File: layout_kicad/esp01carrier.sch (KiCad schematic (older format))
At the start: 17 parts, among them J1 ESP-01, J2 REED1, J3 REED2, J4 Vin 5V, U1 CD74HCT86E, U2 SN74HCT32N, U3 HT7333

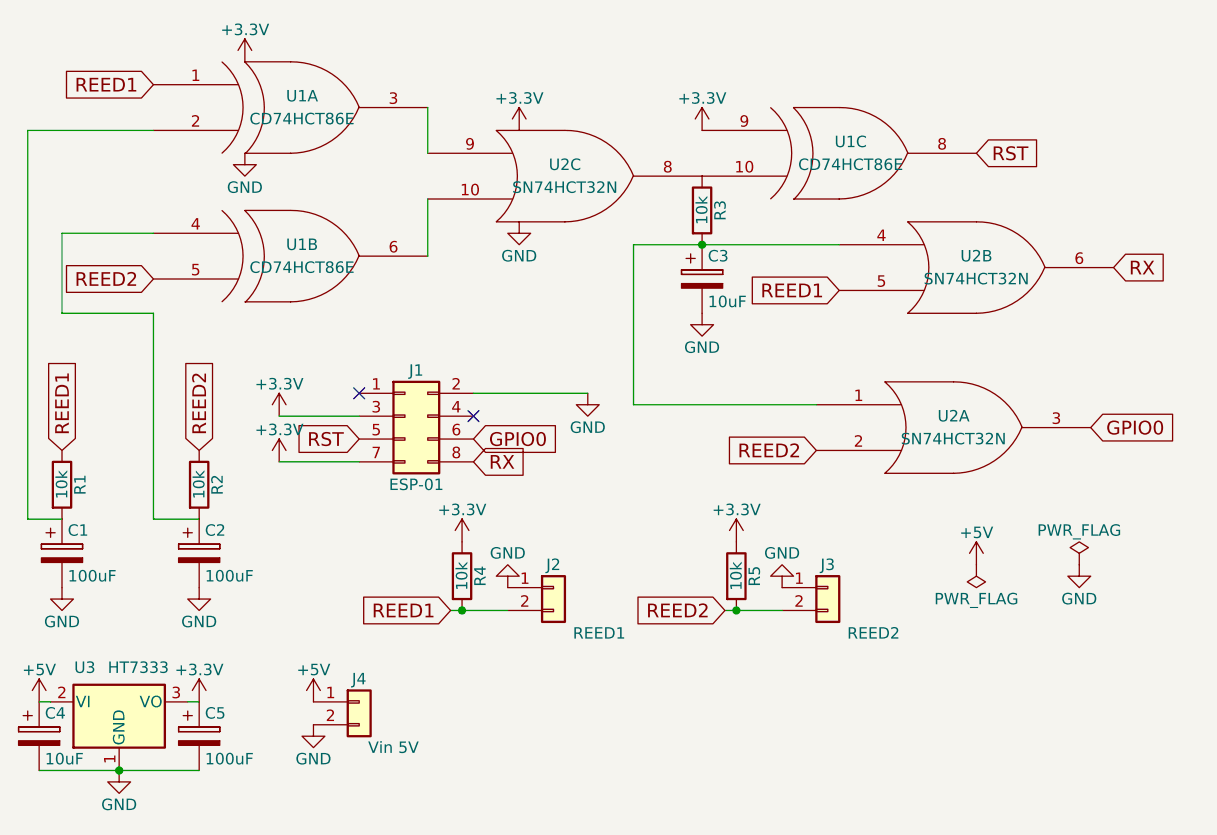
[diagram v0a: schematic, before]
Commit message: Change RC-curcuits to reduce current
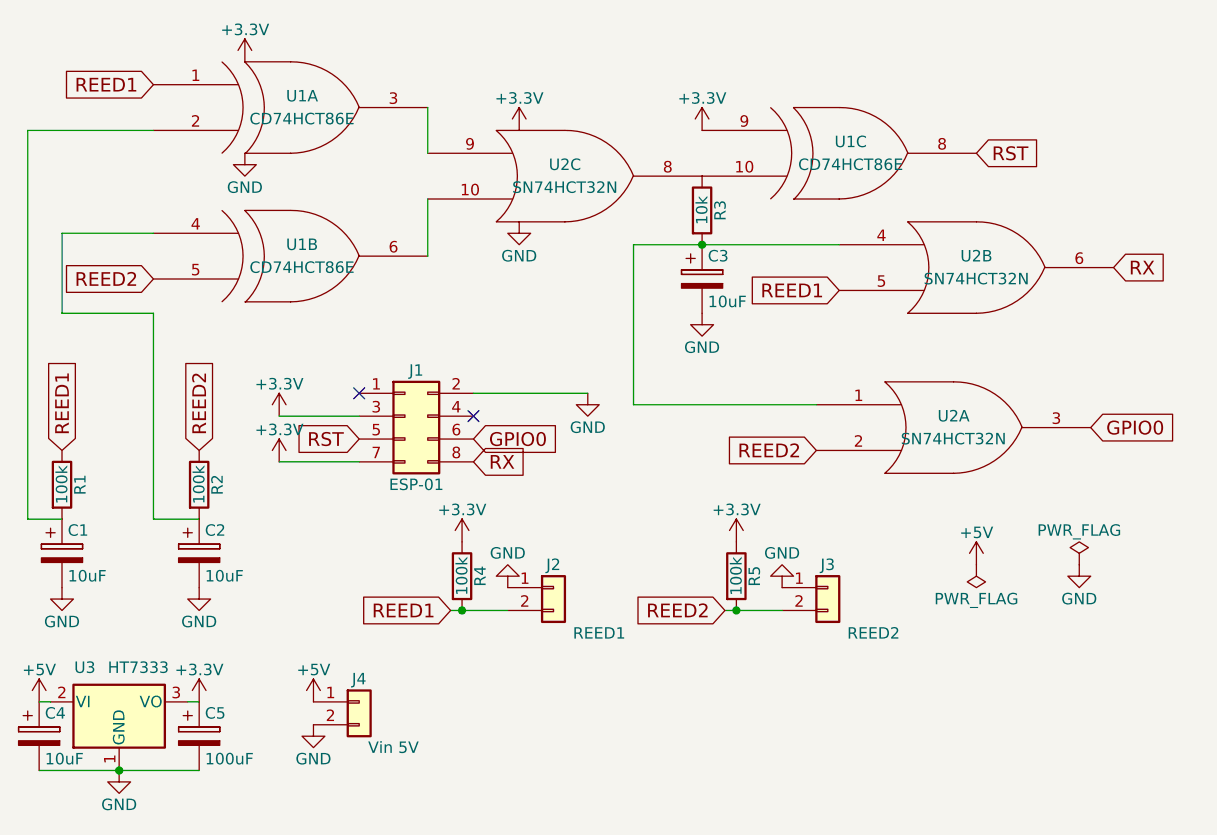
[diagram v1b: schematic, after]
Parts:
- C1, C2: value 100uF -> 10uF
- R1, R2, R4, R5: value 10k -> 100k
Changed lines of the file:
@@
 P 1300 3450
 F 0 "C1" H 1325 3550 50  0000 L CNN
-F 1 "100uF" H 1325 3350 50  0000 L CNN
+F 1 "10uF" H 1325 3350 50  0000 L CNN
 F 2 "Capacitors_THT:CP_Radial_D7.5mm_P2.50mm" H 1338 3300 50  0001 C CNN
 F 3 "" H 1300 3450 50  0001 C CNN
@@
 P 1900 3450
 F 0 "C2" H 1925 3550 50  0000 L CNN
-F 1 "100uF" H 1925 3350 50  0000 L CNN
+F 1 "10uF" H 1925 3350 50  0000 L CNN
 F 2 "Capacitors_THT:CP_Radial_D7.5mm_P2.50mm" H 1938 3300 50  0001 C CNN
 F 3 "" H 1900 3450 50  0001 C CNN
@@
 P 1300 3150
 F 0 "R1" V 1380 3150 50  0000 C CNN
-F 1 "10k" V 1300 3150 50  0000 C CNN
+F 1 "100k" V 1300 3150 50  0000 C CNN
 F 2 "Resistors_THT:R_Axial_DIN0207_L6.3mm_D2.5mm_P7.62mm_Horizontal" V 1230 3150 50  0001 C CNN
 F 3 "" H 1300 3150 50  0001 C CNN
@@
 P 1900 3150
 F 0 "R2" V 1980 3150 50  0000 C CNN
-F 1 "10k" V 1900 3150 50  0000 C CNN
+F 1 "100k" V 1900 3150 50  0000 C CNN
 F 2 "Resistors_THT:R_Axial_DIN0207_L6.3mm_D2.5mm_P7.62mm_Horizontal" V 1830 3150 50  0001 C CNN
 F 3 "" H 1900 3150 50  0001 C CNN
@@
 P 3050 3550
 F 0 "R4" V 3130 3550 50  0000 C CNN
-F 1 "10k" V 3050 3550 50  0000 C CNN
+F 1 "100k" V 3050 3550 50  0000 C CNN
 F 2 "Resistors_THT:R_Axial_DIN0207_L6.3mm_D2.5mm_P7.62mm_Horizontal" V 2980 3550 50  0001 C CNN
 F 3 "" H 3050 3550 50  0001 C CNN
@@
 P 4250 3550
 F 0 "R5" V 4330 3550 50  0000 C CNN
-F 1 "10k" V 4250 3550 50  0000 C CNN
+F 1 "100k" V 4250 3550 50  0000 C CNN
 F 2 "Resistors_THT:R_Axial_DIN0207_L6.3mm_D2.5mm_P7.62mm_Horizontal" V 4180 3550 50  0001 C CNN
 F 3 "" H 4250 3550 50  0001 C CNN
